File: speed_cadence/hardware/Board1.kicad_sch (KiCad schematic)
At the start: 17 parts, among them IC1 AH1912-W-7, J1 DX07S016JA3R1500, J2 Conn_01x04_Pin, J3 Conn_ST_STDC14, J4 XT60_M_7.2mm, SW1 SW_Push, U1 STM32F042G6U6TR, U2 TS2940CW33_RPG

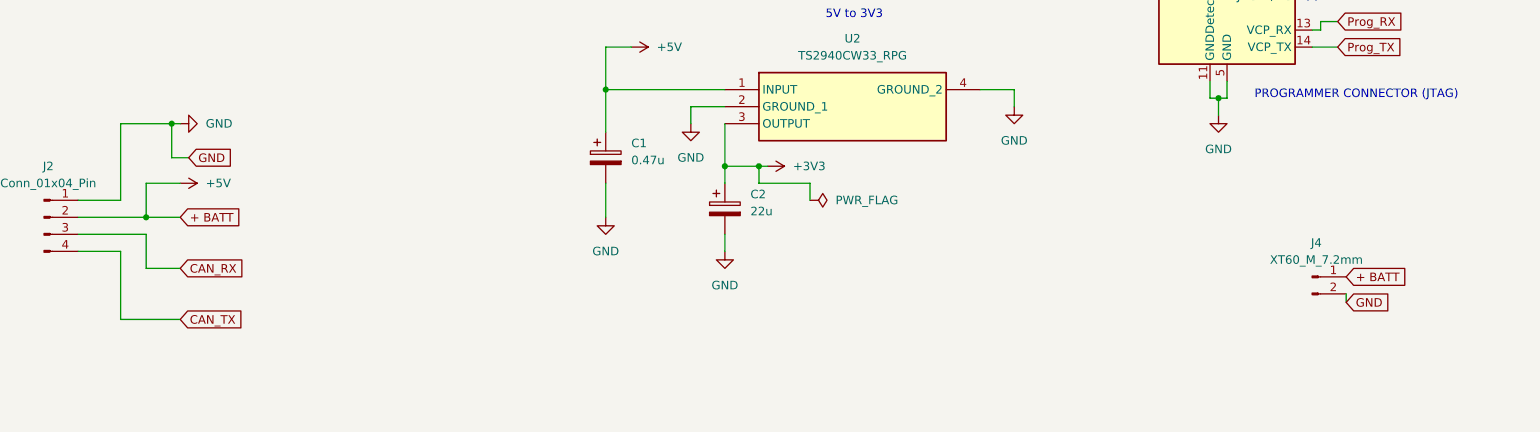
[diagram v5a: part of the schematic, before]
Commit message: Removed battery connector
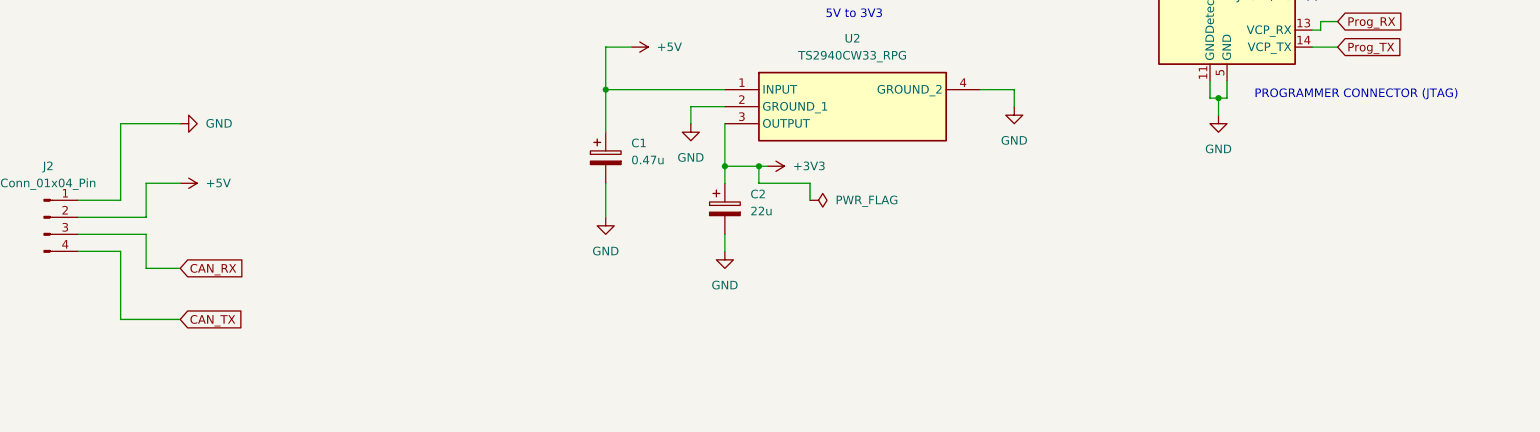
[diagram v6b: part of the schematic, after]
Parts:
- removed J4: XT60_M_7.2mm, Connector_AMASS:AMASS_XT60-M_1x02_P7.20mm_Vertical, symbol Connector:Conn_01x02_Pin
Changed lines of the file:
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@@
 	)
 	(junction
-		(at 46.99 128.27)
-		(diameter 0)
-		(color 0 0 0 0)
-	)
-	(junction
 		(at 129.54 134.62)
 		(diameter 0)
@@
 	)
 	(junction
-		(at 43.18 142.24)
-		(diameter 0)
-		(color 0 0 0 0)
-	)
-	(junction
 		(at 49.53 58.42)
 		(diameter 0)
@@
 	(wire
 		(pts
-			(xy 43.18 142.24) (xy 48.26 142.24)
-		)
-		(stroke
-			(width 0)
-			(type default)
-		)
-	)
-	(wire
-		(pts
 			(xy 142.24 137.16) (xy 134.62 137.16)
 		)
@@
 	(wire
 		(pts
-			(xy 222.25 153.67) (xy 222.25 154.94)
-		)
-		(stroke
-			(width 0)
-			(type default)
-		)
-	)
-	(wire
-		(pts
 			(xy 49.53 40.64) (xy 49.53 46.99)
 		)
@@
 	(wire
 		(pts
-			(xy 46.99 128.27) (xy 48.26 128.27)
-		)
-		(stroke
-			(width 0)
-			(type default)
-		)
-	)
-	(wire
-		(pts
 			(xy 223.52 62.23) (xy 226.06 62.23)
 		)
@@
 	(wire
 		(pts
-			(xy 39.37 128.27) (xy 46.99 128.27)
+			(xy 39.37 128.27) (xy 48.26 128.27)
 		)
 		(stroke
@@
 	(wire
 		(pts
-			(xy 46.99 133.35) (xy 49.53 133.35)
-		)
-		(stroke
-			(width 0)
-			(type default)
-		)
-	)
-	(wire
-		(pts
 			(xy 134.62 137.16) (xy 134.62 134.62)
 		)
@@
 	(wire
 		(pts
-			(xy 46.99 128.27) (xy 46.99 133.35)
-		)
-		(stroke
-			(width 0)
-			(type default)
-		)
-	)
-	(wire
-		(pts
 			(xy 167.64 123.19) (xy 172.72 123.19)
 		)
@@
 		)
 	)
-	(global_label "+ BATT"
-		(shape input)
-		(at 48.26 142.24 0)
-		(fields_autoplaced yes)
-		(effects
-			(font
-				(size 1.27 1.27)
-			)
-			(justify left)
-		)
-		(property "Intersheetrefs" "${INTERSHEET_REFS}"
-			(at 58.079 142.24 0)
-			(effects
-				(font
-					(size 1.27 1.27)
-				)
-				(justify left)
-				(hide yes)
-			)
-		)
-	)
 	(global_label "Prog_RX"
 		(shape input)
@@
 		)
 	)
-	(global_label "GND"
-		(shape input)
-		(at 49.53 133.35 0)
-		(fields_autoplaced yes)
-		(effects
-			(font
-				(size 1.27 1.27)
-			)
-			(justify left)
-		)
-		(property "Intersheetrefs" "${INTERSHEET_REFS}"
-			(at 56.3857 133.35 0)
-			(effects
-				(font
-					(size 1.27 1.27)
-				)
-				(justify left)
-				(hide yes)
-			)
-		)
-	)
 	(global_label "Prog_RX"
 		(shape input)
@@
 		)
 	)
-	(global_label "+ BATT"
-		(shape input)
-		(at 222.25 151.13 0)
-		(fields_autoplaced yes)
-		(effects
-			(font
-				(size 1.27 1.27)
-			)
-			(justify left)
-		)
-		(property "Intersheetrefs" "${INTERSHEET_REFS}"
-			(at 232.069 151.13 0)
-			(effects
-				(font
-					(size 1.27 1.27)
-				)
-				(justify left)
-				(hide yes)
-			)
-		)
-	)
-	(global_label "GND"
-		(shape input)
-		(at 222.25 154.94 0)
-		(fields_autoplaced yes)
-		(effects
-			(font
-				(size 1.27 1.27)
-			)
-			(justify left)
-		)
-		(property "Intersheetrefs" "${INTERSHEET_REFS}"
-			(at 229.1057 154.94 0)
-			(effects
-				(font
-					(size 1.27 1.27)
-				)
-				(justify left)
-				(hide yes)
-			)
-		)
-	)
 	(symbol
 		(lib_id "Mechanical:MountingHole")
@@
 				)
 			)
-		)
-	)
-	(symbol
-		(lib_id "Connector:Conn_01x02_Pin")
-		(at 217.17 151.13 0)
-		(unit 1)
-		(exclude_from_sim no)
-		(in_bom yes)
-		(on_board yes)
-		(dnp no)
-		(fields_autoplaced yes)
-		(property "Reference" "J4"
-			(at 217.805 146.05 0)
-			(effects
-				(font
-					(size 1.27 1.27)
-				)
-			)
-		)
-		(property "Value" "XT60_M_7.2mm"
-			(at 217.805 148.59 0)
-			(effects
-				(font
-					(size 1.27 1.27)
-				)
-			)
-		)
-		(property "Footprint" "Connector_AMASS:AMASS_XT60-M_1x02_P7.20mm_Vertical"
-			(at 217.17 151.13 0)
-			(effects
-				(font
-					(size 1.27 1.27)
-				)
-				(hide yes)
-			)
-		)
-		(property "Datasheet" "~"
-			(at 217.17 151.13 0)
-			(effects
-				(font
-					(size 1.27 1.27)
-				)
-				(hide yes)
-			)
-		)
-		(property "Description" "Generic connector, single row, 01x02, script generated"
-			(at 217.17 151.13 0)
-			(effects
-				(font
-					(size 1.27 1.27)
-				)
-				(hide yes)
-			)
-		)
-		(pin "2"
-		)
-		(pin "1"
-		)
-		(instances
-			(project "Board1"
-				(path "/10163266-8018-4064-a980-f3c4e9dfe9d4"
-					(reference "J4")
-					(unit 1)
-				)
-			)

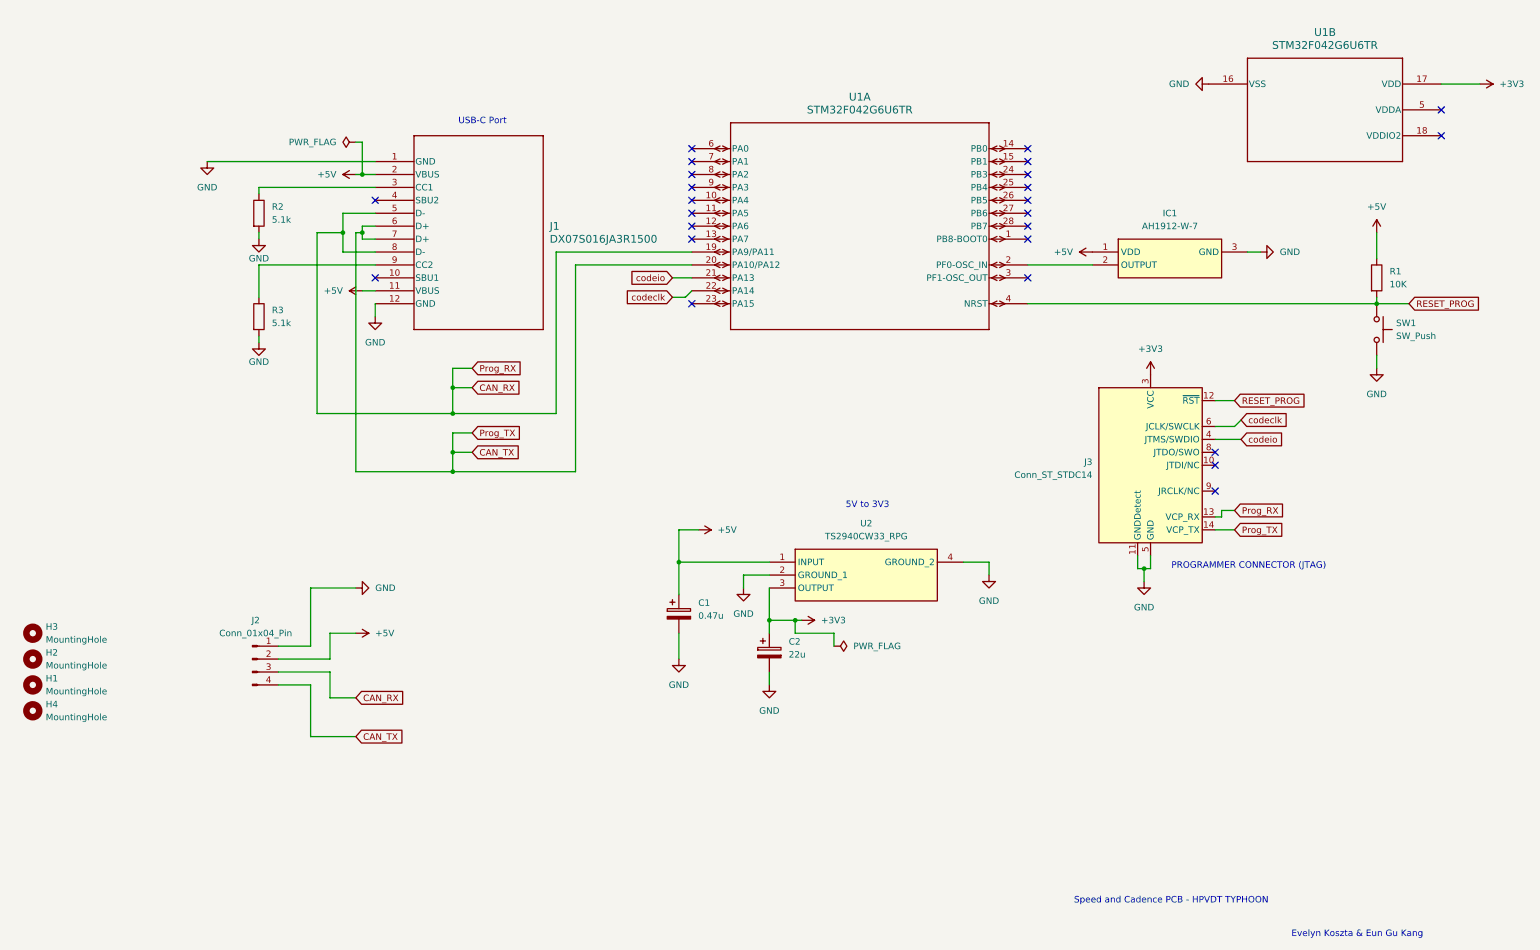
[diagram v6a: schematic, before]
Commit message: Added the CAN transciever
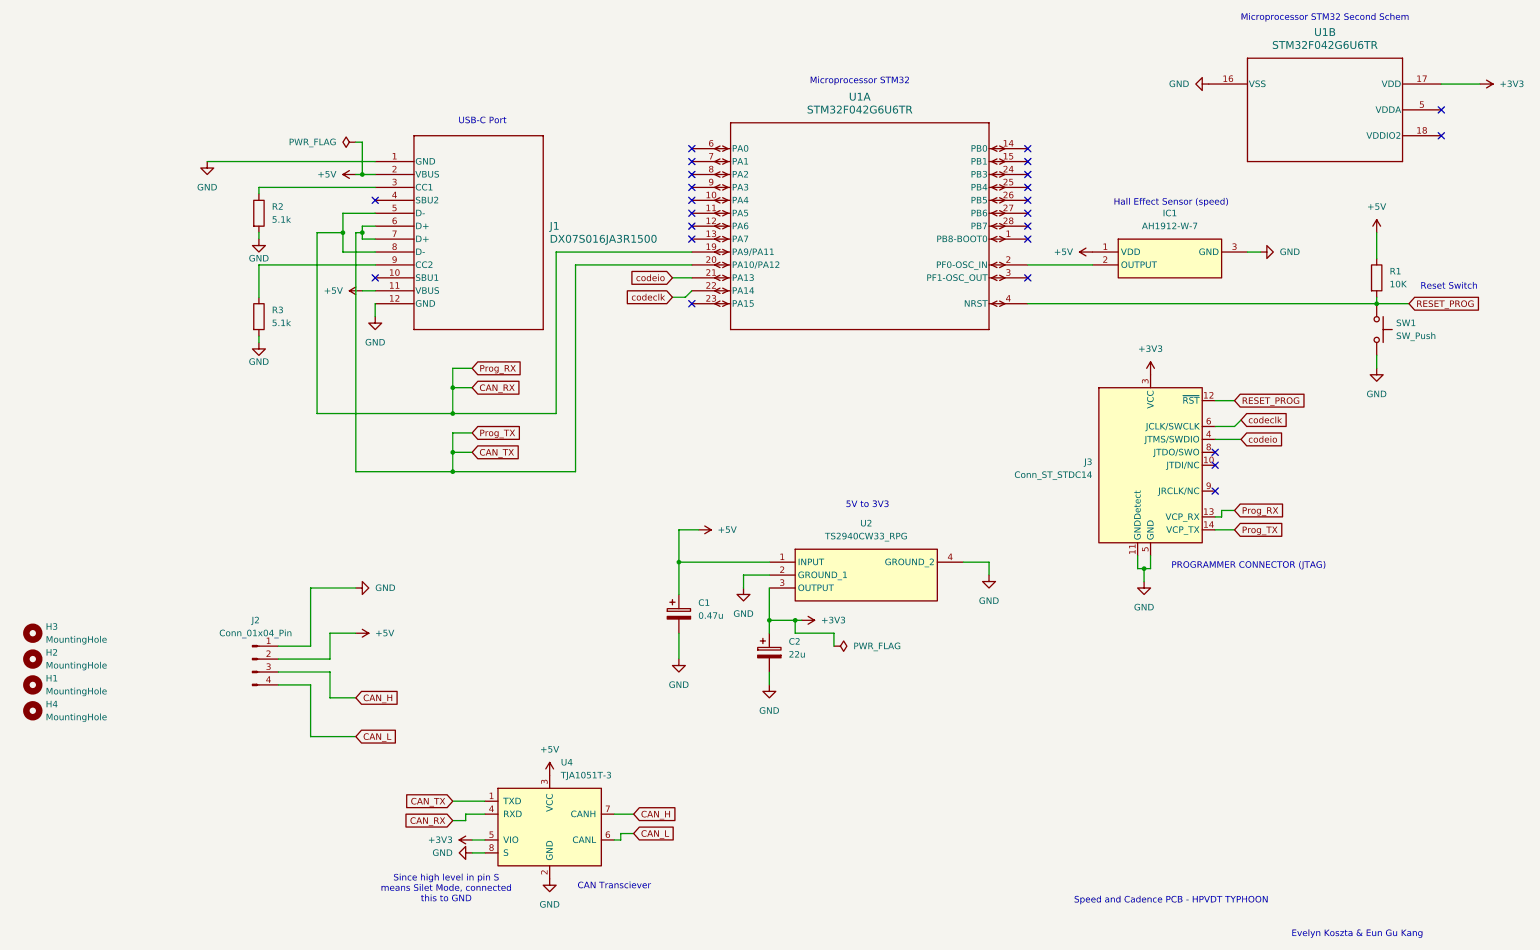
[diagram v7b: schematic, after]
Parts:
- added U4: TJA1051T-3, Package_SO:SOIC-8_3.9x4.9mm_P1.27mm, symbol Interface_CAN_LIN:TJA1051T-3
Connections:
- net +3V3: now also U4.5 (VIO)
- net +5V: now also U4.3 (VCC)
- net CAN_RX: now also U4.4 (RXD); no longer J2.3 (Pin_3)
- net CAN_TX: now also U4.1 (TXD); no longer J2.4 (Pin_4)
- net GND: now also U4.2 (GND), U4.8 (S)
- new net CAN_H: J2.3 (Pin_3), U4.7 (CANH)
- new net CAN_L: J2.4 (Pin_4), U4.6 (CANL)
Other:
- note added: "CAN Transciever"
- note added: "Hall Effect Sensor (speed)"
- note added: "Microprocessor STM32"
- note added: "Microprocessor STM32 Second Schem"
- note added: "Reset Switch"
- note added: "Since high level in pin S means Silet Mode, connected this to GND"

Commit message: Updated board
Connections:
- net CAN_RX: now also U1.20 (PA10/PA12); no longer J1.5 (D-), J1.8 (D-), J3.13 (VCP_RX), U1.19 (PA9/PA11)
- net CAN_TX: now also U1.19 (PA9/PA11); no longer J1.6 (D+), J1.7 (D+), J3.14 (VCP_TX), U1.20 (PA10/PA12)
- net Prog_RX: now reaches U1.8 (PA2)
- net Prog_RX: now also J3.13 (VCP_RX)
- net Prog_TX: now reaches U1.9 (PA3)
- net Prog_TX: now also J3.14 (VCP_TX)
- no-connect marks 25 -> 27
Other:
- note added: "Since high level in pin 8 (s) means Silet Mode, connected this to GND"
- note removed: "Evelyn Koszta & Eun Gu Kang"
- note removed: "Microprocessor STM32 Second Schem"
- note removed: "Since high level in pin S means Silet Mode, connected this to GND"
- note removed: "Speed and Cadence PCB - HPVDT TYPHOON"
- company: (none) -> By Evelyn Koszta and Eun Gu Kang
- title: (none) -> Speed Measurement Board
- moved on the sheet: C1, C2, H1, H2, H3, H4, IC1, J2, J3, R1, R2, R3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
